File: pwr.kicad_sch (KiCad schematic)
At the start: 29 parts, among them U1 AP1501_3.3, U2 AP1501_5, U3 AP1501_ADJ_7.5

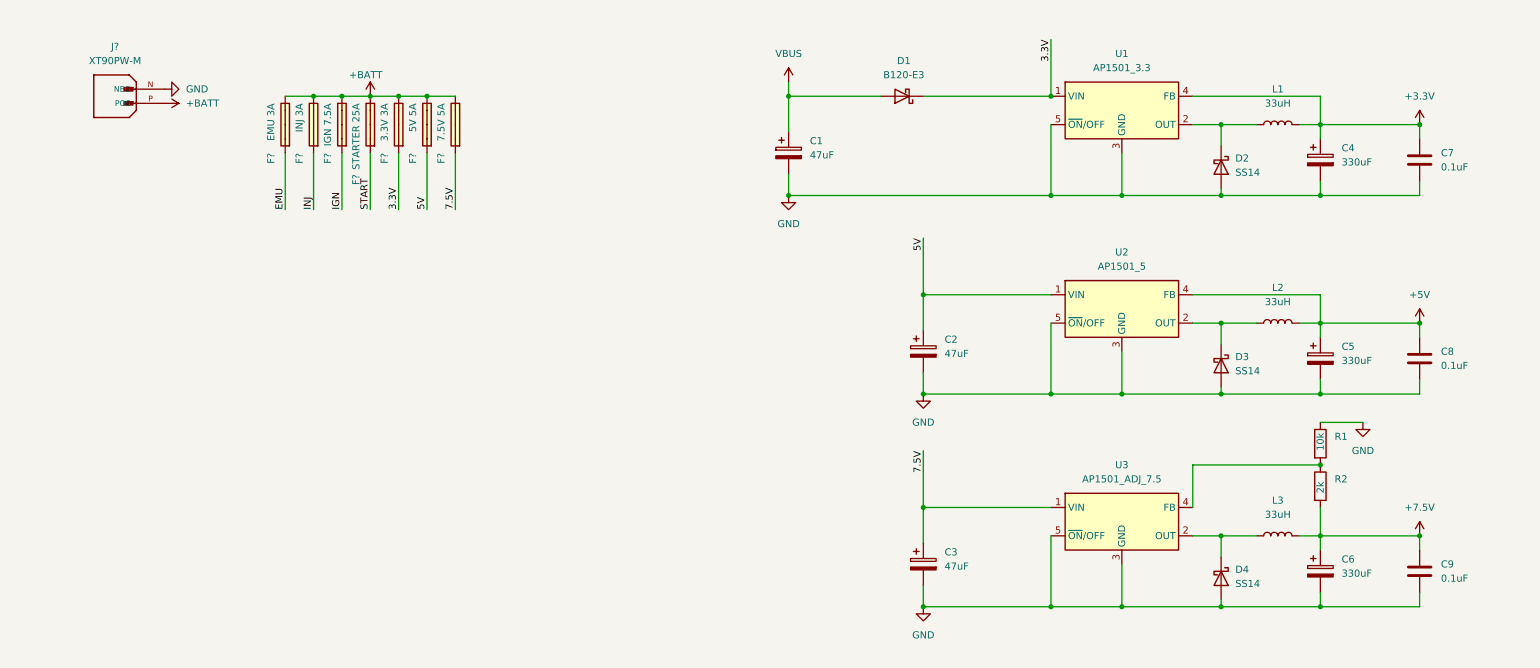
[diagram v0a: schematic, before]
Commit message: Expanded IO
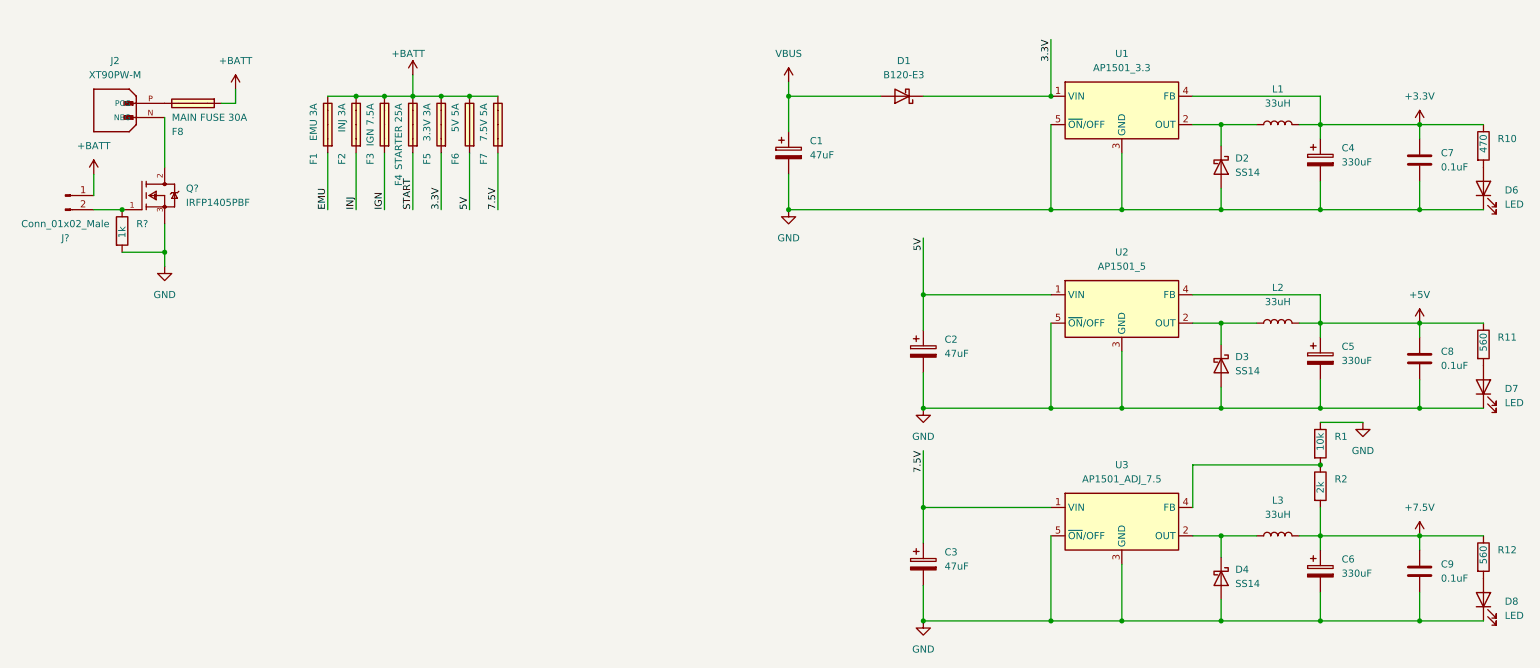
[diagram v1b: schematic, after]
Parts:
- added D6, D7, D8: LED, symbol Device:LED
- added F8: MAIN FUSE 30A, FUSE_3557-2:FUSE_3557-2, symbol 3557-2:3557-2
- added J?: Conn_01x02_Male, symbol Connector:Conn_01x02_Male
- added Q?: IRFP1405PBF, Infineon-PG-TO247-3-0-901-*, symbol IRFP1405:IRFP1405PBF
- added R10: 470, symbol Device:R
- added R11, R12: 560, symbol Device:R
- added R?: 1k, symbol Device:R
- F1, F2, F3, F4, F5, F6, F7: renamed from F?; footprint FUSE_3557-2 -> FUSE_3557-2:FUSE_3557-2
- J2: renamed from J?; footprint AMASS_XT90PW-M -> XT90PW-M:AMASS_XT90PW-M
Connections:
- net +3.3V: now also R10.1
- net +5V: now also R11.1
- net +7.5V: now also R12.1
- net +BATT: now also F8.1, J?.1 (Pin_1); no longer J2.P (POS)
- net GND: now also D6.1 (K), D7.1 (K), D8.1 (K), Q?.3 (S), R?.2; no longer J2.N (NEG)
- new net: D6.2 (A), R10.2
- new net: J?.2 (Pin_2), Q?.1 (G), R?.1
- new net: D8.2 (A), R12.2
- new net: J2.N (NEG), Q?.2 (D)
- new net: F8.3, J2.P (POS)
- new net: D7.2 (A), R11.2
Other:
- title: (none) -> Iron Warriors v2.0 
- moved on the sheet: F1, F2, F3, F4, F5, F6, F7, J2

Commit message: Rev 1.0
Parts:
- C1, C2, C3: footprint (none) -> Capacitor_SMD:CP_Elec_6.3x5.8
- C4, C5, C6: footprint (none) -> Capacitor_SMD:CP_Elec_10x10
- C7, C8, C9: footprint (none) -> Capacitor_SMD:C_0201_0603Metric
- D2, D3, D4: footprint (none) -> Diode_SMD:D_0201_0603Metric
- D6, D7, D8: footprint (none) -> LED_SMD:LED_0201_0603Metric
- J5: renamed from J?; value Conn_01x02_Male -> SAFETY; footprint (none) -> Connector_Molex:Molex_PicoBlade_53047-0210_1x02_P1.25mm_Vertical
- L1, L2, L3: footprint (none) -> Inductor_SMD:L_Bourns_SRR1208_12.7x12.7mm
- Q1: renamed from Q?; footprint Infineon-PG-TO247-3-0-901-* -> IRFP1405:TO247AC
- R1, R10, R11, R12, R2: footprint (none) -> Resistor_SMD:R_0603_1608Metric
- R13: renamed from R?; footprint (none) -> Resistor_SMD:R_0603_1608Metric
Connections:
- net START renamed STARTER
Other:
- moved on the sheet: F1, F2, F3, F4, F5, F6, F7

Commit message: Initial PCB view
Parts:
- C7, C8, C9: footprint Capacitor_SMD:C_0201_0603Metric -> Capacitor_SMD:C_0603_1608Metric
- D2, D3, D4: footprint Diode_SMD:D_0201_0603Metric -> Diode_SMD:D_0603_1608Metric
- D6, D7, D8: footprint LED_SMD:LED_0201_0603Metric -> LED_SMD:LED_0603_1608Metric
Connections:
- net GND: now also Q1.2 (D); no longer Q1.3 (S), R13.2
- net at J2.N (NEG): now also Q1.3 (S), R13.2; no longer Q1.2 (D)
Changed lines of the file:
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@@
   (title_block
     (title "Iron Warriors v2.0 ")
-    (date "2022-12-08")
+    (date "2022-12-13")
     (rev "1.0")
   )
@@
   (junction (at 175.26 88.9) (diameter 0) (color 0 0 0 0)
   )
-  (junction (at 39.37 60.96) (diameter 0) (color 0 0 0 0)
-  )
   (junction (at 246.38 38.1) (diameter 0) (color 0 0 0 0)
   )
@@
   (junction (at 175.26 127) (diameter 0) (color 0 0 0 0)
   )
+  (junction (at 39.37 63.5) (diameter 0) (color 0 0 0 0)
+  )
   (junction (at 97.79 31.75) (diameter 0) (color 0 0 0 0)
   )
@@
     (stroke (width 0) (type default) (color 0 0 0 0))
   )
+  (wire (pts (xy 58.42 63.5) (xy 58.42 36.83))
+    (stroke (width 0) (type default) (color 0 0 0 0))
+  )
   (wire (pts (xy 198.12 111.76) (xy 198.12 127))
     (stroke (width 0) (type default) (color 0 0 0 0))
@@
     (stroke (width 0) (type default) (color 0 0 0 0))
   )
+  (wire (pts (xy 39.37 55.88) (xy 39.37 63.5))
+    (stroke (width 0) (type default) (color 0 0 0 0))
+  )
   (wire (pts (xy 198.12 22.86) (xy 198.12 33.02))
     (stroke (width 0) (type default) (color 0 0 0 0))
@@
     (stroke (width 0) (type default) (color 0 0 0 0))
   )
-  (wire (pts (xy 39.37 63.5) (xy 39.37 60.96))
-    (stroke (width 0) (type default) (color 0 0 0 0))
-  )
   (wire (pts (xy 210.82 88.9) (xy 228.6 88.9))
     (stroke (width 0) (type default) (color 0 0 0 0))
@@
     (stroke (width 0) (type default) (color 0 0 0 0))
   )
+  (wire (pts (xy 58.42 36.83) (xy 39.37 36.83))
+    (stroke (width 0) (type default) (color 0 0 0 0))
+  )
   (wire (pts (xy 228.6 111.76) (xy 223.52 111.76))
     (stroke (width 0) (type default) (color 0 0 0 0))
   )
-  (wire (pts (xy 31.75 60.96) (xy 39.37 60.96))
+  (wire (pts (xy 31.75 63.5) (xy 39.37 63.5))
     (stroke (width 0) (type default) (color 0 0 0 0))
   )
@@
     (stroke (width 0) (type default) (color 0 0 0 0))
   )
-  (wire (pts (xy 39.37 60.96) (xy 39.37 55.88))
-    (stroke (width 0) (type default) (color 0 0 0 0))
-  )
   (wire (pts (xy 246.38 106.68) (xy 246.38 111.76))
     (stroke (width 0) (type default) (color 0 0 0 0))
@@
     (stroke (width 0) (type default) (color 0 0 0 0))
   )
-  (wire (pts (xy 39.37 45.72) (xy 39.37 36.83))
-    (stroke (width 0) (type default) (color 0 0 0 0))
-  )
   (wire (pts (xy 151.13 53.34) (xy 198.12 53.34))
     (stroke (width 0) (type default) (color 0 0 0 0))
@@
     (stroke (width 0) (type default) (color 0 0 0 0))
   )
+  (wire (pts (xy 48.26 45.72) (xy 39.37 45.72))
+    (stroke (width 0) (type default) (color 0 0 0 0))
+  )
   (wire (pts (xy 97.79 31.75) (xy 102.87 31.75))
     (stroke (width 0) (type default) (color 0 0 0 0))
@@
     (stroke (width 0) (type default) (color 0 0 0 0))
   )
+  (wire (pts (xy 31.75 63.5) (xy 31.75 60.96))
+    (stroke (width 0) (type default) (color 0 0 0 0))
+  )
   (wire (pts (xy 198.12 127) (xy 210.82 127))
     (stroke (width 0) (type default) (color 0 0 0 0))
@@
   )
   (wire (pts (xy 234.95 111.76) (xy 228.6 111.76))
+    (stroke (width 0) (type default) (color 0 0 0 0))
+  )
+  (wire (pts (xy 39.37 63.5) (xy 58.42 63.5))
     (stroke (width 0) (type default) (color 0 0 0 0))
   )
@@
     (effects (font (size 1.27 1.27)) (justify left bottom))
   )
+  (hierarchical_label "STARTER" (shape output) (at 97.79 52.07 270)
+    (effects (font (size 1.27 1.27)) (justify right))
+  )
+  (hierarchical_label "INJ" (shape output) (at 87.63 52.07 270)
+    (effects (font (size 1.27 1.27)) (justify right))
+  )
+  (hierarchical_label "EMU" (shape output) (at 82.55 52.07 270)
+    (effects (font (size 1.27 1.27)) (justify right))
+  )
+  (hierarchical_label "IGN" (shape output) (at 92.71 52.07 270)
+    (effects (font (size 1.27 1.27)) (justify right))
+  )
   (symbol (lib_id "Device:LED") (at 275.59 49.53 90) (unit 1)
     (in_bom yes) (on_board yes) (fields_autoplaced)
@@
       (effects (font (size 1.27 1.27)) (justify right))
     )
-    (property "Footprint" "LED_SMD:LED_0201_0603Metric" (id 2) (at 275.59 49.53 0)
+    (property "Footprint" "LED_SMD:LED_0603_1608Metric" (id 2) (at 275.59 49.53 0)
       (effects (font (size 1.27 1.27)) hide)
     )
@@
       (effects (font (size 1.27 1.27)) (justify left))
     )
-    (property "Footprint" "Diode_SMD:D_0201_0603Metric" (id 2) (at 228.6 45.72 0)
+    (property "Footprint" "Diode_SMD:D_0603_1608Metric" (id 2) (at 228.6 45.72 0)
       (effects (font (size 1.27 1.27)) hide)
     )
@@
       (effects (font (size 1.27 1.27)) (justify right))
     )
-    (property "Footprint" "LED_SMD:LED_0201_0603Metric" (id 2) (at 275.59 123.19 0)
+    (property "Footprint" "LED_SMD:LED_0603_1608Metric" (id 2) (at 275.59 123.19 0)
       (effects (font (size 1.27 1.27)) hide)
     )
@@
       (effects (font (size 1.27 1.27)) (justify left))
     )
-    (property "Footprint" "Diode_SMD:D_0201_0603Metric" (id 2) (at 228.6 81.28 0)
+    (property "Footprint" "Diode_SMD:D_0603_1608Metric" (id 2) (at 228.6 81.28 0)
       (effects (font (size 1.27 1.27)) hide)
     )
@@
       (effects (font (size 1.27 1.27)) (justify right))
     )
-    (property "Footprint" "LED_SMD:LED_0201_0603Metric" (id 2) (at 275.59 85.09 0)
+    (property "Footprint" "LED_SMD:LED_0603_1608Metric" (id 2) (at 275.59 85.09 0)
       (effects (font (size 1.27 1.27)) hide)
     )
@@
       (effects (font (size 1.27 1.27)) (justify left))
     )
-    (property "Footprint" "Capacitor_SMD:C_0201_0603Metric" (id 2) (at 265.1252 121.92 0)
+    (property "Footprint" "Capacitor_SMD:C_0603_1608Metric" (id 2) (at 265.1252 121.92 0)
       (effects (font (size 1.27 1.27)) hide)
     )
@@
       (effects (font (size 1.27 1.27)) (justify left))
     )
-    (property "Footprint" "Capacitor_SMD:C_0201_0603Metric" (id 2) (at 265.1252 83.82 0)
+    (property "Footprint" "Capacitor_SMD:C_0603_1608Metric" (id 2) (at 265.1252 83.82 0)
       (effects (font (size 1.27 1.27)) hide)
     )
@@
     (pin "1")
   )
+  (symbol (lib_id "power:GND") (at 48.26 45.72 0) (unit 1)
+    (in_bom yes) (on_board yes)
+    (property "Reference" "#PWR0142" (id 0) (at 48.26 52.07 0)
+      (effects (font (size 1.27 1.27)) hide)
+    )
+    (property "Value" "GND" (id 1) (at 50.8 48.26 0)
+      (effects (font (size 1.27 1.27)) (justify left))
+    )
+    (property "Footprint" "" (id 2) (at 48.26 45.72 0)
+      (effects (font (size 1.27 1.27)) hide)
+    )
+    (property "Datasheet" "" (id 3) (at 48.26 45.72 0)
+      (effects (font (size 1.27 1.27)) hide)
+    )
+    (pin "1")
+  )
   (symbol (lib_id "Device:R") (at 246.38 102.87 0) (unit 1)
     (in_bom yes) (on_board yes)
@@
       (effects (font (size 1.27 1.27)) (justify left))
     )
-    (property "Footprint" "Diode_SMD:D_0201_0603Metric" (id 2) (at 228.6 119.38 0)
+    (property "Footprint" "Diode_SMD:D_0603_1608Metric" (id 2) (at 228.6 119.38 0)
       (effects (font (size 1.27 1.27)) hide)
     )
@@
       (effects (font (size 1.27 1.27)) (justify left))
     )
-    (property "Footprint" "Capacitor_SMD:C_0201_0603Metric" (id 2) (at 265.1252 48.26 0)
+    (property "Footprint" "Capacitor_SMD:C_0603_1608Metric" (id 2) (at 265.1252 48.26 0)
       (effects (font (size 1.27 1.27)) hide)
     )
@@
     (pin "2")
   )
-  (symbol (lib_id "power:GND") (at 39.37 63.5 0) (unit 1)
-    (in_bom yes) (on_board yes) (fields_autoplaced)
-    (property "Reference" "#PWR02" (id 0) (at 39.37 69.85 0)
-      (effects (font (size 1.27 1.27)) hide)
-    )
-    (property "Value" "GND" (id 1) (at 39.37 68.58 0))
-    (property "Footprint" "" (id 2) (at 39.37 63.5 0)
-      (effects (font (size 1.27 1.27)) hide)
-    )
-    (property "Datasheet" "" (id 3) (at 39.37 63.5 0)
-      (effects (font (size 1.27 1.27)) hide)
-    )
-    (pin "1")
-  )
   (symbol (lib_id "Device:R") (at 31.75 57.15 0) (unit 1)

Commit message: First full version of the PCB
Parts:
- J5: footprint Connector_Molex:Molex_PicoBlade_53047-0210_1x02_P1.25mm_Vertical -> TerminalBlock_Phoenix:TerminalBlock_Phoenix_MPT-0,5-2-2.54_1x02_P2.54mm_Horizontal
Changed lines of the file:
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@@
     (property "Reference" "J5" (id 0) (at 21.59 58.42 0))
     (property "Value" "SAFETY" (id 1) (at 21.59 55.88 0))
-    (property "Footprint" "Connector_Molex:Molex_PicoBlade_53047-0210_1x02_P1.25mm_Vertical" (id 2) (at 21.59 50.8 0)
+    (property "Footprint" "TerminalBlock_Phoenix:TerminalBlock_Phoenix_MPT-0,5-2-2.54_1x02_P2.54mm_Horizontal" (id 2) (at 21.59 50.8 0)
       (effects (font (size 1.27 1.27)) hide)
     )

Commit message: Small corrections
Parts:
- added D11: B120-E3, Diode_SMD:D_SMA, symbol Diode:B120-E3
- added F9: 7.5V 5A, FUSE_3557-2:FUSE_3557-2, symbol 3557-2:3557-2
- D2, D3, D4: footprint Diode_SMD:D_0603_1608Metric -> Diode_SMD:D_SMA
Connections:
- net +BATT: now also J5.2 (Pin_2), F9.3; no longer J5.1 (Pin_1)
- net 3.3V: now also D11.2 (A); no longer D1.1 (K), U1.1 (VIN)
- net VBUS: no longer C1.1
- net at Q1.1 (G), R13.1: now also J5.1 (Pin_1); no longer J5.2 (Pin_2)
- new net: C1.1, D1.1 (K), D11.1 (K), U1.1 (VIN)
- new net 16V: F9.1

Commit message: Added CAN transsiver to RP2040
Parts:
- F9: value 7.5V 5A -> 16V 5A
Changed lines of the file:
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@@
       (effects (font (size 1.27 1.27)) (justify right))
     )
-    (property "Value" "7.5V 5A" (id 1) (at 115.57 33.02 0)
+    (property "Value" "16V 5A" (id 1) (at 115.57 33.02 0)
       (effects (font (size 1.27 1.27)) (justify right))
     )
